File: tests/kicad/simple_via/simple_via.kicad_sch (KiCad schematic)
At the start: 2 parts

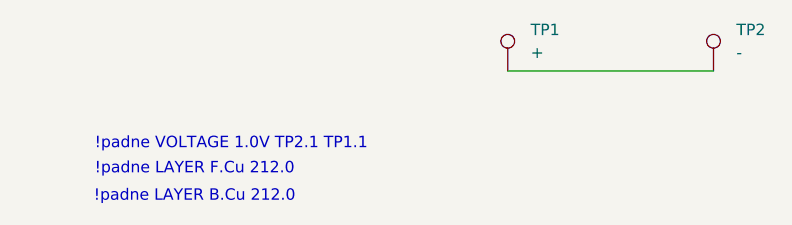
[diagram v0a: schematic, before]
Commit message: feat: Rudimentary stackup spec support
Still veeeeeery TBD
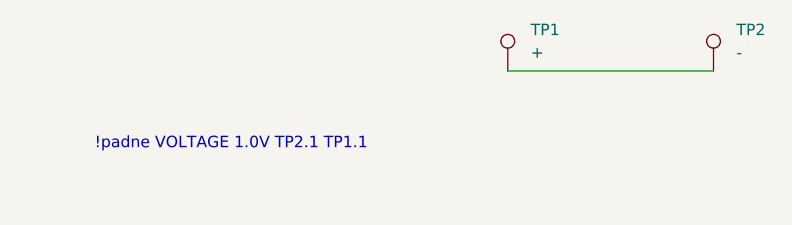
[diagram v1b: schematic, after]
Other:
- note removed: "!padne LAYER B.Cu 212.0"
- note removed: "!padne LAYER F.Cu 212.0"
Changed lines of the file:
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@@
-		)
-	)
-	(text "!padne LAYER F.Cu 212.0"
-		(exclude_from_sim no)
-		(at 98.552 85.852 0)
-		(effects
-			(font
-				(size 1.27 1.27)
-			)
-		)
-	)
-	(text "!padne LAYER B.Cu 212.0"
-		(exclude_from_sim no)
-		(at 98.552 88.9 0)
-		(effects
-			(font
-				(size 1.27 1.27)
-			)
 		)
 	)

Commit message: feat: Richer directive syntax
This commit adds support for named directive parameters. No more
guessing which parameter is the positive terminal positive and which is the
negative terminal!
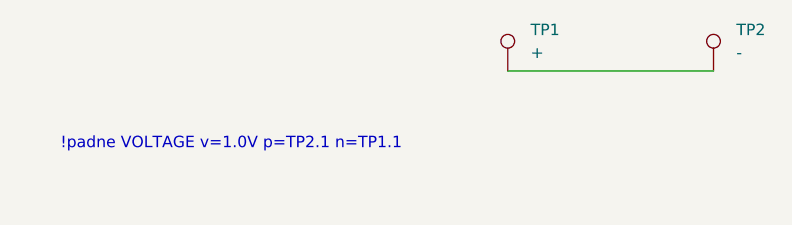
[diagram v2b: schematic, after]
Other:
- note added: "!padne VOLTAGE v=1.0V p=TP2.1 n=TP1.1"
- note removed: "!padne VOLTAGE 1.0V TP2.1 TP1.1"
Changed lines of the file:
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@@
 		)
 	)
-	(text "!padne VOLTAGE 1.0V TP2.1 TP1.1"
+	(text "!padne VOLTAGE v=1.0V p=TP2.1 n=TP1.1"
 		(exclude_from_sim no)
 		(at 102.616 83.058 0)
